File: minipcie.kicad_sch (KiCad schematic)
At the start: 0 parts

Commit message: PMIC DCDC
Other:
- title: Leaf RV1126 Power -> Leaf RV1126 PMIC RK809
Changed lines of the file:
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@@
   (paper "A4")
   (title_block
-    (title "Leaf RV1126 Power")
+    (title "Leaf RV1126 PMIC RK809")
     (date "2023-02-23")
     (rev "1")

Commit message: updated: PMIC codec
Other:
- title: Leaf RV1126 PMIC RK809 -> Leaf RV1126 PMIC RK809 Codec
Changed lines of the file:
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@@
   (paper "A4")
   (title_block
-    (title "Leaf RV1126 PMIC RK809")
-    (date "2023-02-23")
+    (title "Leaf RV1126 PMIC RK809 Codec")
+    (date "2023-02-25")
     (rev "1")
     (company "Qingdao IotPi Information Technology")

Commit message: updated: titles
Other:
- title: Leaf RV1126 PMIC RK809 Codec -> Leaf RV1126 RK809 mini PCIe
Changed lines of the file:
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@@
   (paper "A4")
   (title_block
-    (title "Leaf RV1126 PMIC RK809 Codec")
+    (title "Leaf RV1126 RK809 mini PCIe")
     (date "2023-02-25")
     (rev "1")

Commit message: added mini pcie board
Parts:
- added J5: mini PCIe Card edge, Leaf_Connector_PCBEdge:PCIe_MiniCard, symbol Connector_Generic:Conn_02x26_Odd_Even
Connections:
- new net mPCIe_1V5: J5.28 (Pin_28), J5.48 (Pin_48), J5.6 (Pin_6)
- new net mPCIe_3V3_aux: J5.2 (Pin_2), J5.24 (Pin_24), J5.39 (Pin_39), J5.41 (Pin_41), J5.52 (Pin_52)
- new net mPCIe_GND: J5.15 (Pin_15), J5.18 (Pin_18), J5.21 (Pin_21), J5.26 (Pin_26), J5.27 (Pin_27), J5.29 (Pin_29), J5.34 (Pin_34), J5.35 (Pin_35), J5.37 (Pin_37), J5.4 (Pin_4), J5.40 (Pin_40), J5.43 (Pin_43), J5.50 (Pin_50), J5.9 (Pin_9)
- new net mPCIe_I2C_SCL: J5.30 (Pin_30)
- new net mPCIe_I2C_SDA: J5.32 (Pin_32)
- new net mPCIe_Reserved: J5.17 (Pin_17), J5.19 (Pin_19), J5.45 (Pin_45), J5.47 (Pin_47), J5.49 (Pin_49), J5.51 (Pin_51)
- new net mPCIe_USB_DM: J5.38 (Pin_38)
- new net mPCIe_USB_DP: J5.36 (Pin_36)

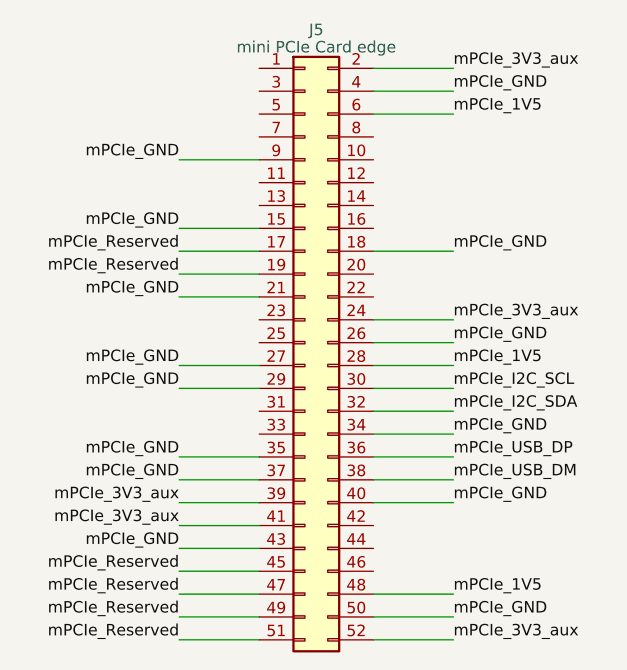
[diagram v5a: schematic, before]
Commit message: fix some ERCs
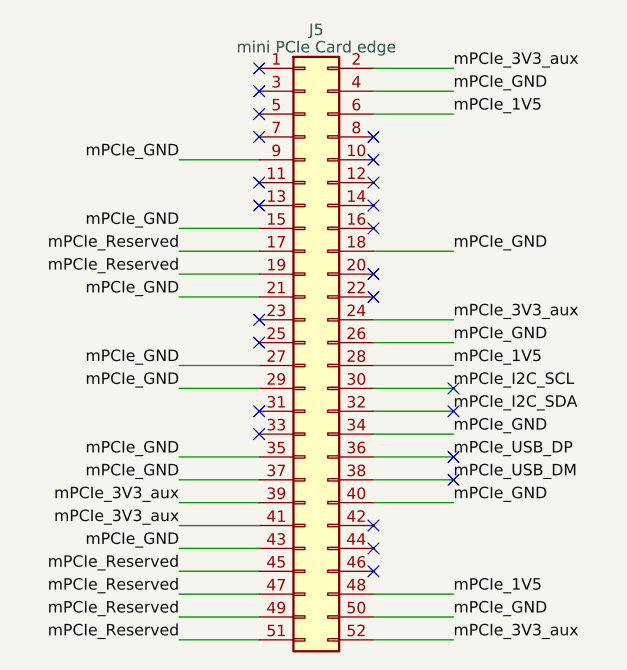
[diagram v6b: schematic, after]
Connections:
- no-connect marks 0 -> 24
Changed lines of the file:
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@@
     (company "Qingdao IotPi Information Technology")
   )
+  (no_connect (at 170.18 50.8))
+  (no_connect (at 191.77 91.44))
+  (no_connect (at 170.18 63.5))
+  (no_connect (at 191.77 83.82))
+  (no_connect (at 182.88 58.42))
+  (no_connect (at 182.88 104.14))
+  (no_connect (at 191.77 86.36))
+  (no_connect (at 170.18 88.9))
+  (no_connect (at 170.18 78.74))
+  (no_connect (at 191.77 93.98))
+  (no_connect (at 182.88 71.12))
+  (no_connect (at 170.18 86.36))
+  (no_connect (at 182.88 73.66))
+  (no_connect (at 170.18 76.2))
+  (no_connect (at 182.88 63.5))
+  (no_connect (at 170.18 60.96))
+  (no_connect (at 182.88 66.04))
+  (no_connect (at 182.88 55.88))
+  (no_connect (at 170.18 55.88))
+  (no_connect (at 170.18 48.26))
+  (no_connect (at 170.18 53.34))
+  (no_connect (at 182.88 60.96))
+  (no_connect (at 182.88 101.6))
+  (no_connect (at 182.88 99.06))
   (wire (pts (xy 170.18 109.22) (xy 161.29 109.22))
     (stroke (width 0) (type default))

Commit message: added OSC, updated annotations
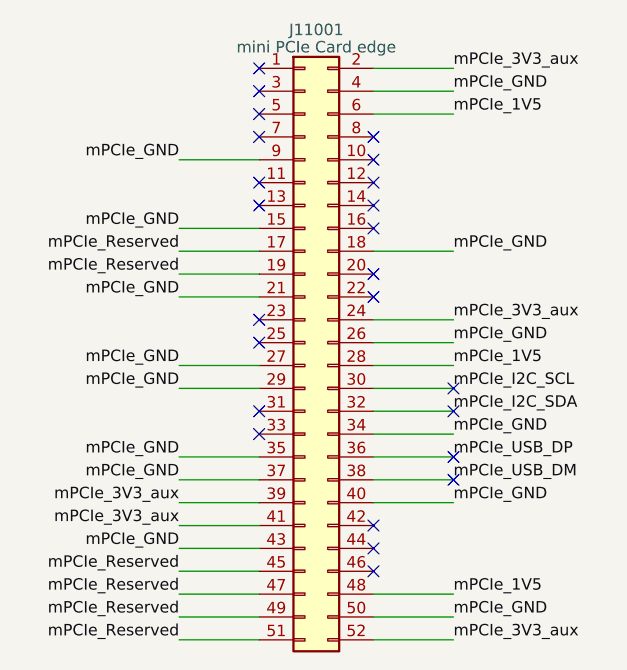
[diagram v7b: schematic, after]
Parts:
- renumbered J5 to J11001
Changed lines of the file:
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@@
   (symbol (lib_id "Connector_Generic:Conn_02x26_Odd_Even") (at 175.26 78.74 0) (unit 1)
     (in_bom yes) (on_board yes) (dnp no) (fields_autoplaced)
-    (property "Reference" "J5" (at 176.53 43.9801 0)
+    (property "Reference" "J11001" (at 176.53 43.9801 0)
       (effects (font (size 1.27 1.27)))
     )
@@
       (project "leaf"
         (path "/e3b58043-16a3-43c8-9fad-9c9784eebfa4/fba3f144-6b35-47ae-b616-9ead32e4b269"
-          (reference "J5") (unit 1)
+          (reference "J11001") (unit 1)
         )
       )

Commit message: move DDR power decoupling capacitors into DDR4 Sheet
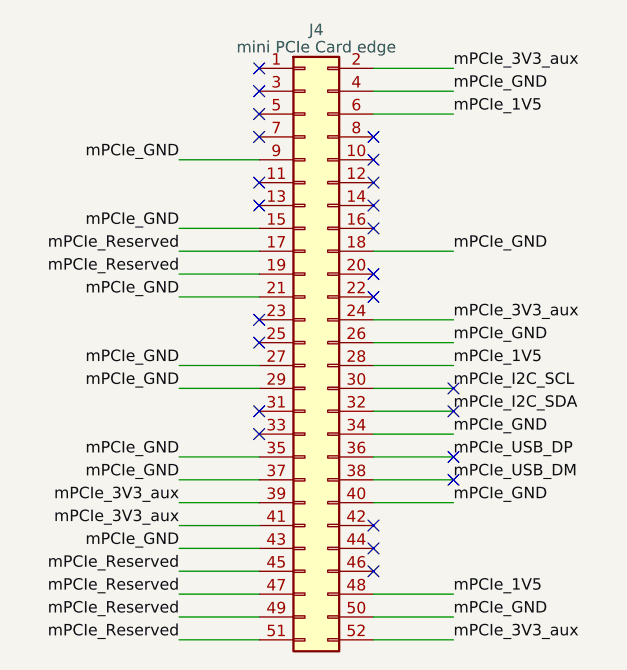
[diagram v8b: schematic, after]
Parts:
- renumbered J11001 to J4
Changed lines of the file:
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@@
   (symbol (lib_id "Connector_Generic:Conn_02x26_Odd_Even") (at 175.26 78.74 0) (unit 1)
     (in_bom yes) (on_board yes) (dnp no) (fields_autoplaced)
-    (property "Reference" "J11001" (at 176.53 43.9801 0)
+    (property "Reference" "J4" (at 176.53 43.9801 0)
       (effects (font (size 1.27 1.27)))
     )
@@
       (project "leaf"
         (path "/e3b58043-16a3-43c8-9fad-9c9784eebfa4/fba3f144-6b35-47ae-b616-9ead32e4b269"
-          (reference "J11001") (unit 1)
+          (reference "J4") (unit 1)
         )
       )
